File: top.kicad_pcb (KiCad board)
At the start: 2 copper layers, 0 parts

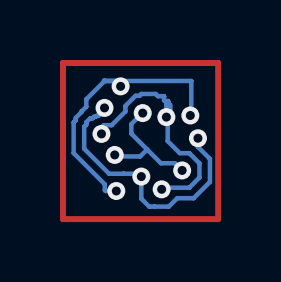
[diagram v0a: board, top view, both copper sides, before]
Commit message: wip via solver
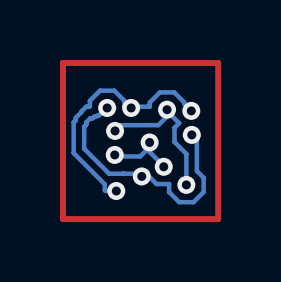
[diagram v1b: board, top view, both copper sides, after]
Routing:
- net Net7: track 8.79 -> 5.59 mm
- net Net5: track 4.39 -> 2.63 mm
- net Net6: track 9.71 -> 8.94 mm
